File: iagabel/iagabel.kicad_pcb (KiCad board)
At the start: 2 copper layers, 42 x 24 mm, 17 parts, among them J1 A2008WR-S-4P, K1 TCUT1300X01, U1 74LVC2G14GW

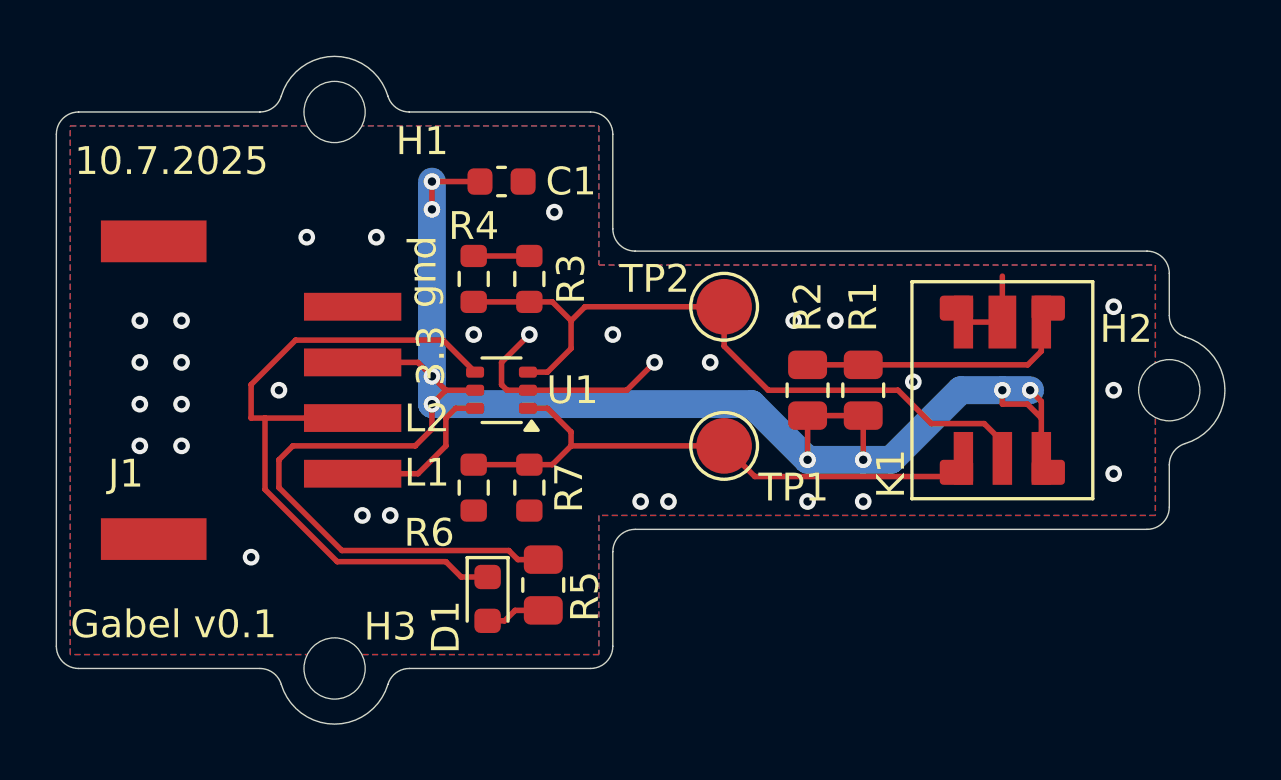
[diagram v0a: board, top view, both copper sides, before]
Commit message: iagabel v0.2: changed indicator led resistor to 470 Ohms, production data
I changed the led resistor to 470 ohm because the led was too bright.
For the production run at jlcpcb i designed a panel with mousebites.
The production at jlcpcb started at 16.9.2025
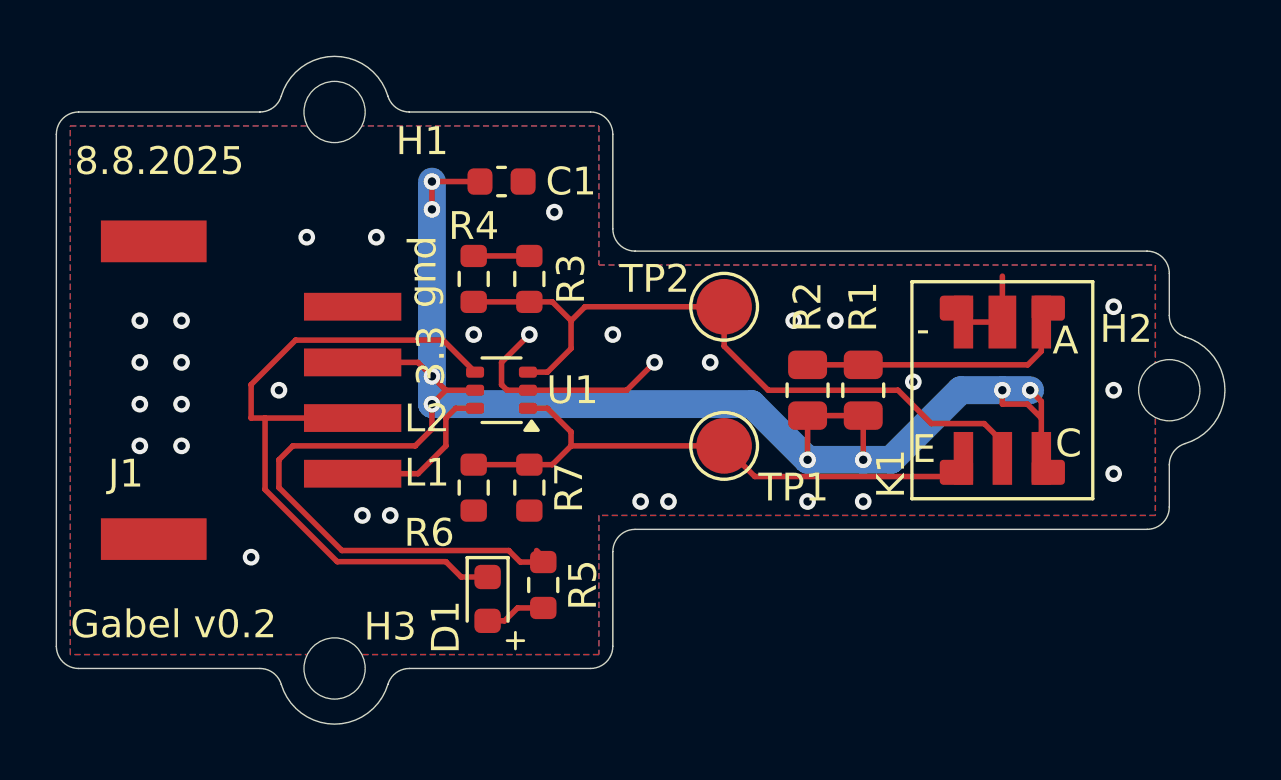
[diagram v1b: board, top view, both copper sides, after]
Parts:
- R1: value 150 -> 150R
- R5: value 120 -> 470R; footprint Resistor_SMD:R_0805_2012Metric -> Resistor_SMD:R_0603_1608Metric
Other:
- board text added: "-"
- board text added: "8.8.2025"
- board text added: "A"
- board text added: "C"
- board text added: "E"
- board text added: "Gabel v0.2"
- board text removed: "10.7.2025"
- board text removed: "Gabel v0.1"
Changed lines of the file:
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@@
 		)
 	)
-	(footprint "Resistor_SMD:R_0805_2012Metric"
+	(footprint "Resistor_SMD:R_0603_1608Metric"
 		(layer "F.Cu")
 		(at 17.5 17 -90)
-		(descr "Resistor SMD 0805 (2012 Metric), square (rectangular) end terminal, IPC-7351 nominal, (Body size source: IPC-SM-782 page 72, https://www.pcb-3d.com/wordpress/wp-content/uploads/ipc-sm-782a_amendment_1_and_2.pdf), generated with kicad-footprint-generator")
+		(descr "Resistor SMD 0603 (1608 Metric), square (rectangular) end terminal, IPC-7351 nominal, (Body size source: IPC-SM-782 page 72, https://www.pcb-3d.com/wordpress/wp-content/uploads/ipc-sm-782a_amendment_1_and_2.pdf), generated with kicad-footprint-generator")
 		(tags "resistor")
 		(property "Reference" "R5"
-			(at 0.4125 -1.5 90)
+			(at 0 -1.43 270)
 			(layer "F.SilkS")
 			(effects
@@
 			)
 		)
-		(property "Value" "120"
-			(at 0 1.65 90)
+		(property "Value" "470R"
+			(at 0 1.43 270)
 			(layer "F.Fab")
 			(effects
@@
 			)
 		)
-		(property "Datasheet" "https://jlcpcb.com/api/file/downloadByFileSystemAccessId/8579706485296709632"
-			(at 0 0 90)
+		(property "Datasheet" "https://jlcpcb.com/api/file/downloadByFileSystemAccessId/8579706265439817728"
+			(at 0 0 270)
 			(layer "F.Fab")
 			(hide yes)
@@
 			)
 		)
-		(property "Description" "UNIROYAL 0805W8F1200T5E 0805 120 Ohm"
-			(at 0 0 90)
+		(property "Description" "UNIROYAL 0603WAF4700T5E 0602 470 Ohm"
+			(at 0 0 270)
 			(layer "F.Fab")
 			(hide yes)
@@
 			)
 		)
-		(property "LCSC part number" "C17437"
+		(property "LCSC part number" "C23179"
 			(at 0 0 270)
 			(unlocked yes)
@@
 		(attr smd)
 		(fp_line
-			(start -0.227064 0.735)
-			(end 0.227064 0.735)
+			(start -0.237258 0.5225)
+			(end 0.237258 0.5225)
 			(stroke
 				(width 0.12)
@@
 		)
 		(fp_line
-			(start -0.227064 -0.735)
-			(end 0.227064 -0.735)
+			(start -0.237258 -0.5225)
+			(end 0.237258 -0.5225)
 			(stroke
 				(width 0.12)
@@
 		)
 		(fp_line
-			(start -1.68 0.95)
-			(end -1.68 -0.95)
+			(start -1.48 0.73)
+			(end -1.48 -0.73)
 			(stroke
 				(width 0.05)
@@
 		)
 		(fp_line
-			(start 1.68 0.95)
-			(end -1.68 0.95)
+			(start 1.48 0.73)
+			(end -1.48 0.73)
 			(stroke
 				(width 0.05)
@@
 		)
 		(fp_line
-			(start -1.68 -0.95)
-			(end 1.68 -0.95)
+			(start -1.48 -0.73)
+			(end 1.48 -0.73)
 			(stroke
 				(width 0.05)
@@
 		)
 		(fp_line
-			(start 1.68 -0.95)
-			(end 1.68 0.95)
+			(start 1.48 -0.73)
+			(end 1.48 0.73)
 			(stroke
 				(width 0.05)
@@
 		)
 		(fp_line
-			(start -1 0.625)
-			(end -1 -0.625)
+			(start -0.8 0.4125)
+			(end -0.8 -0.4125)
 			(stroke
 				(width 0.1)
@@
 		)
 		(fp_line
-			(start 1 0.625)
-			(end -1 0.625)
+			(start 0.8 0.4125)
+			(end -0.8 0.4125)
 			(stroke
 				(width 0.1)
@@
 		)
 		(fp_line
-			(start -1 -0.625)
-			(end 1 -0.625)
+			(start -0.8 -0.4125)
+			(end 0.8 -0.4125)
 			(stroke
 				(width 0.1)
@@
 		)
 		(fp_line
-			(start 1 -0.625)
-			(end 1 0.625)
+			(start 0.8 -0.4125)
+			(end 0.8 0.4125)
 			(stroke
 				(width 0.1)
@@
 		)
 		(fp_text user "${REFERENCE}"
-			(at 0 0 90)
+			(at 0 0 270)
 			(layer "F.Fab")
 			(effects
 				(font
-					(size 0.5 0.5)
-					(thickness 0.08)
+					(size 0.4 0.4)
+					(thickness 0.06)
 				)
 			)
 		)
 		(pad "1" smd roundrect
-			(at -0.9125 0 270)
-			(size 1.025 1.4)
+			(at -0.825 0 270)
+			(size 0.8 0.95)
 			(layers "F.Cu" "F.Mask" "F.Paste")
-			(roundrect_rratio 0.243902)
+			(roundrect_rratio 0.25)
 			(net 1 "+3.3V")
 			(pintype "passive")
 		)
 		(pad "2" smd roundrect
-			(at 0.9125 0 270)
-			(size 1.025 1.4)
+			(at 0.825 0 270)
+			(size 0.8 0.95)
 			(layers "F.Cu" "F.Mask" "F.Paste")
-			(roundrect_rratio 0.243902)
+			(roundrect_rratio 0.25)
 			(net 4 "Net-(D1-A)")
 			(pintype "passive")
 		)
 		(embedded_fonts no)
-		(model "${KICAD9_3DMODEL_DIR}/Resistor_SMD.3dshapes/R_0805_2012Metric.step"
+		(model "${KICAD9_3DMODEL_DIR}/Resistor_SMD.3dshapes/R_0603_1608Metric.step"
 			(offset
 				(xyz 0 0 0)
@@
 			)
 		)
-		(property "Datasheet" ""
+		(property "Datasheet" "~"
 			(at 0 0 0)
 			(layer "F.Fab")
@@
 			)
 		)
-		(property "Datasheet" ""
+		(property "Datasheet" "~"
 			(at 0 0 0)
 			(unlocked yes)
@@
 			)
 		)
-		(property "Value" "150"
+		(property "Value" "150R"
 			(at 0 1.65 90)
 			(layer "F.Fab")
@@
 			)
 		)
-		(property "Datasheet" ""
+		(property "Datasheet" "~"
 			(at 0 0 0)
 			(layer "F.Fab")
@@
 			)
 		)
-		(property "Datasheet" ""
+		(property "Datasheet" "~"
 			(at 0 0 0)
 			(unlocked yes)
@@
 			)
 		)
-		(property "Datasheet" ""
+		(property "Datasheet" "~"
 			(at 0 0 0)
 			(layer "F.Fab")
@@
 	)
 	(gr_line
+		(start 16.5 18.7)
+		(end 16.5 19.3)
+		(stroke
+			(width 0.1)
+			(type default)
+		)
+		(layer "F.SilkS")
+	)
+	(gr_line
+		(start 16.2 19)
+		(end 16.8 19)
+		(stroke
+			(width 0.1)
+			(type default)
+		)
+		(layer "F.SilkS")
+	)
+	(gr_line
 		(start 40 7.311333)
 		(end 40 5.799999)
@@
 		(layer "Edge.Cuts")
 	)
+	(gr_text "C"
+		(at 35.9 12.5 0)
+		(layer "F.SilkS")
+		(effects
+			(font
+				(size 1 1)
+				(thickness 0.15)
+			)
+			(justify left bottom)
+		)
+	)
 	(gr_text "gnd"
 		(at 13.75 7.05 90)
@@
 		)
 	)
+	(gr_text "E"
+		(at 30.75 12.7 0)
+		(layer "F.SilkS")
+		(effects
+			(font
+				(size 1 1)
+				(thickness 0.15)
+			)
+			(justify left bottom)
+		)
+	)
+	(gr_text "-"
+		(at 30.9 8.4 0)
+		(layer "F.SilkS")
+		(effects
+			(font
+				(size 1 1)
+				(thickness 0.15)
+			)
+			(justify left bottom)
+		)
+	)
+	(gr_text "A"
+		(at 35.8 8.8 0)
+		(layer "F.SilkS")
+		(effects
+			(font
+				(size 1 1)
+				(thickness 0.15)
+			)
+			(justify left bottom)
+		)
+	)
 	(gr_text "3.3"
 		(at 14.05 9.85 90)
@@
 		)
 	)
-	(gr_text "10.7.2025"
+	(gr_text "8.8.2025"
 		(at 0.65 2.35 0)
 		(layer "F.SilkS")
@@
 		)
 	)
-	(gr_text "Gabel v0.1"
+	(gr_text "Gabel v0.2"
 		(at 0.5 19 0)
 		(layer "F.SilkS")
@@
 	)
 	(segment
+		(start 16.2615 15.7615)
+		(end 16.675 16.175)
+		(width 0.2)
+		(layer "F.Cu")
+		(net 1)
+	)
+	(segment
 		(start 34 10)
 		(end 34 10.5)
@@
 	)
 	(segment
-		(start 13.5 11.4)
-		(end 13.5 10.5)
-		(width 0.2)
-		(layer "F.Cu")
-		(net 1)
-	)
-	(segment
 		(start 29 12.5)
 		(end 29 10.9125)
@@
 	)
 	(segment
-		(start 8 13.5)
-		(end 8 12.5)
-		(width 0.2)
-		(layer "F.Cu")
-		(net 1)
-	)
-	(segment
-		(start 16.5875 16.0875)
-		(end 16.2615 15.7615)
-		(width 0.2)
-		(layer "F.Cu")
-		(net 1)
-	)
-	(segment
-		(start 8.5 12)
+		(start 13.5 11.4)
 		(end 12.9 12)
 		(width 0.2)
@@
 	)
 	(segment
-		(start 8 12.5)
-		(end 8.5 12)
-		(width 0.2)
-		(layer "F.Cu")
-		(net 1)
-	)
-	(segment
 		(start 13.5 2.5)
 		(end 13.5 3.5)
@@
 	)
 	(segment
-		(start 17.5 16.0875)
-		(end 16.5875 16.0875)
+		(start 8.5 12)
+		(end 8 12.5)
 		(width 0.2)
 		(layer "F.Cu")
@@
 	)
 	(segment
-		(start 12.9 12)
-		(end 13.5 11.4)
+		(start 10.2615 15.7615)
+		(end 16.2615 15.7615)
+		(width 0.2)
+		(layer "F.Cu")
+		(net 1)
+	)
+	(segment
+		(start 8 12.5)
+		(end 8 13.5)
 		(width 0.2)
 		(layer "F.Cu")
@@
 	)
 	(segment
+		(start 8 13.5)
+		(end 10.2615 15.7615)
+		(width 0.2)
+		(layer "F.Cu")
+		(net 1)
+	)
+	(segment
 		(start 34.9 10.5)
 		(end 35.4 11)
@@
 	)
 	(segment
-		(start 10.2615 15.7615)
-		(end 8 13.5)
+		(start 16.675 16.175)
+		(end 17.5 16.175)
 		(width 0.2)
 		(layer "F.Cu")
@@
 	)
 	(segment
+		(start 12.9 12)
+		(end 8.5 12)
+		(width 0.2)
+		(layer "F.Cu")
+		(net 1)
+	)
+	(segment
 		(start 34 10.5)
 		(end 34.9 10.5)
@@
 	)
 	(segment
-		(start 16.2615 15.7615)
-		(end 10.2615 15.7615)
+		(start 13.5 9.5)
+		(end 13 9)
 		(width 0.2)
 		(layer "F.Cu")
@@
 	(segment
 		(start 13.5 9.5)
-		(end 13 9)
+		(end 14 10)
 		(width 0.2)
 		(layer "F.Cu")
@@
 	)
 	(segment
-		(start 13.5 9.5)
-		(end 14 10)
+		(start 13.5 10.5)
+		(end 13.5 11.4)
 		(width 0.2)
 		(layer "F.Cu")
@@
 	)
 	(segment
-		(start 16.4875 17.9125)
-		(end 17.5 17.9125)
+		(start 15.5 18.2875)
+		(end 16.1125 18.2875)
 		(width 0.2)
 		(layer "F.Cu")
@@
 	)
 	(segment
-		(start 15.5 18.2875)
-		(end 16.1125 18.2875)
+		(start 16.575 17.825)
+		(end 17.5 17.825)
 		(width 0.2)
 		(layer "F.Cu")
@@
 	(segment
 		(start 16.1125 18.2875)
-		(end 16.4875 17.9125)
+		(end 16.575 17.825)
 		(width 0.2)
 		(layer "F.Cu")
